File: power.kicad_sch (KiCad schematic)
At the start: 30 parts, among them J7 Conn_01x02, Q1 CSD17311Q5, Q2 CSD17311Q5, Q4 2N7002K, U10 DS4432U+, U8 INA260, U9 TPS40305

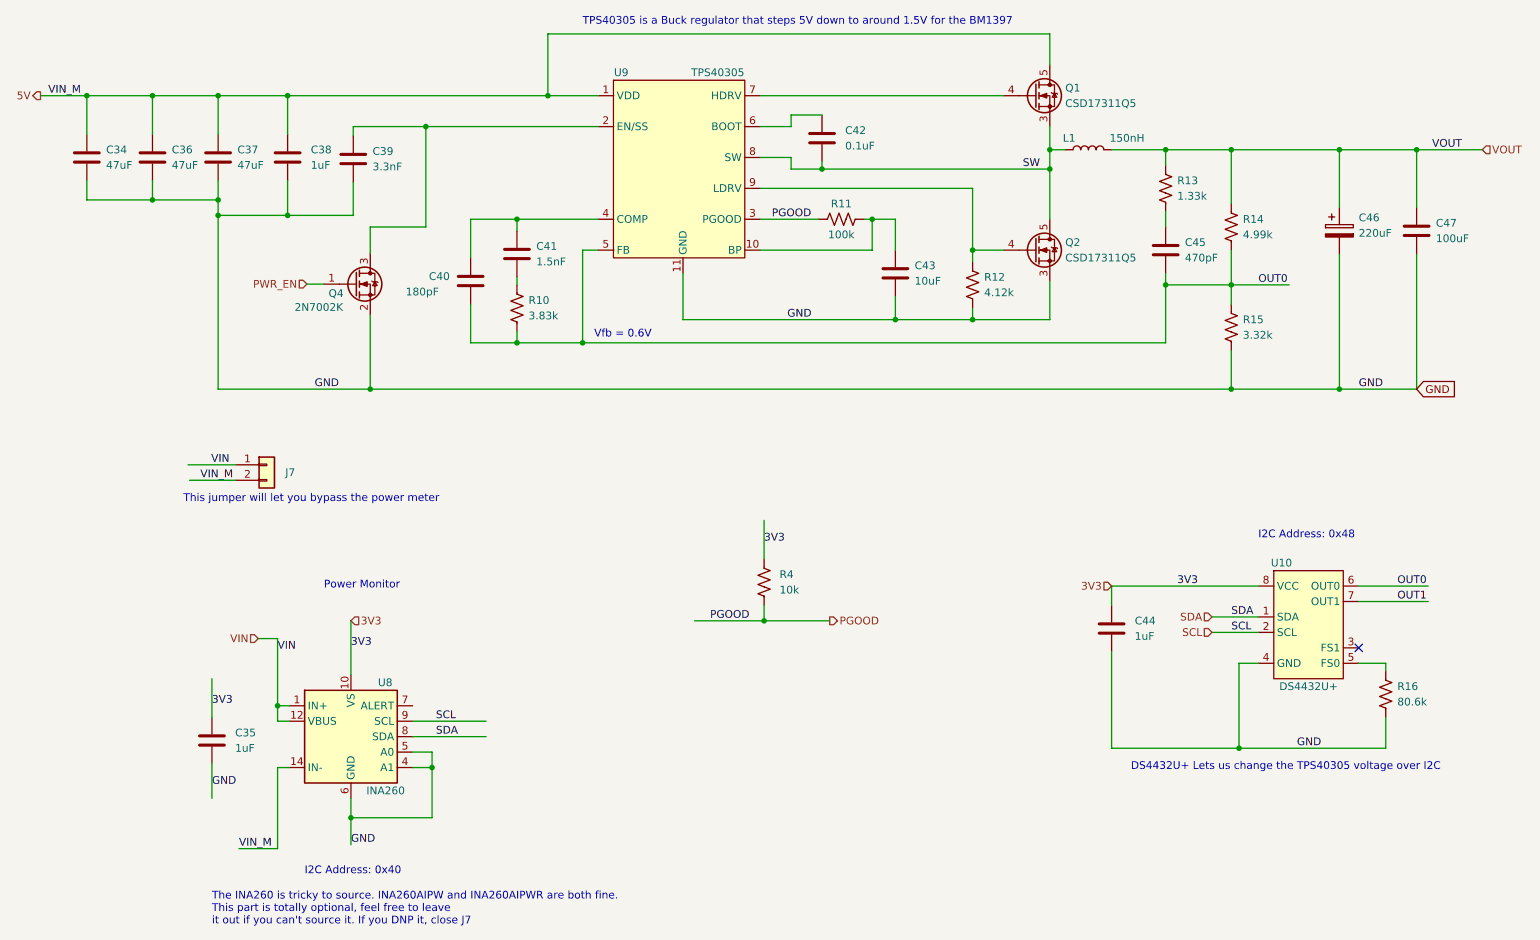
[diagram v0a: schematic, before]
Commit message: added bitaxe variant for rasperry pi
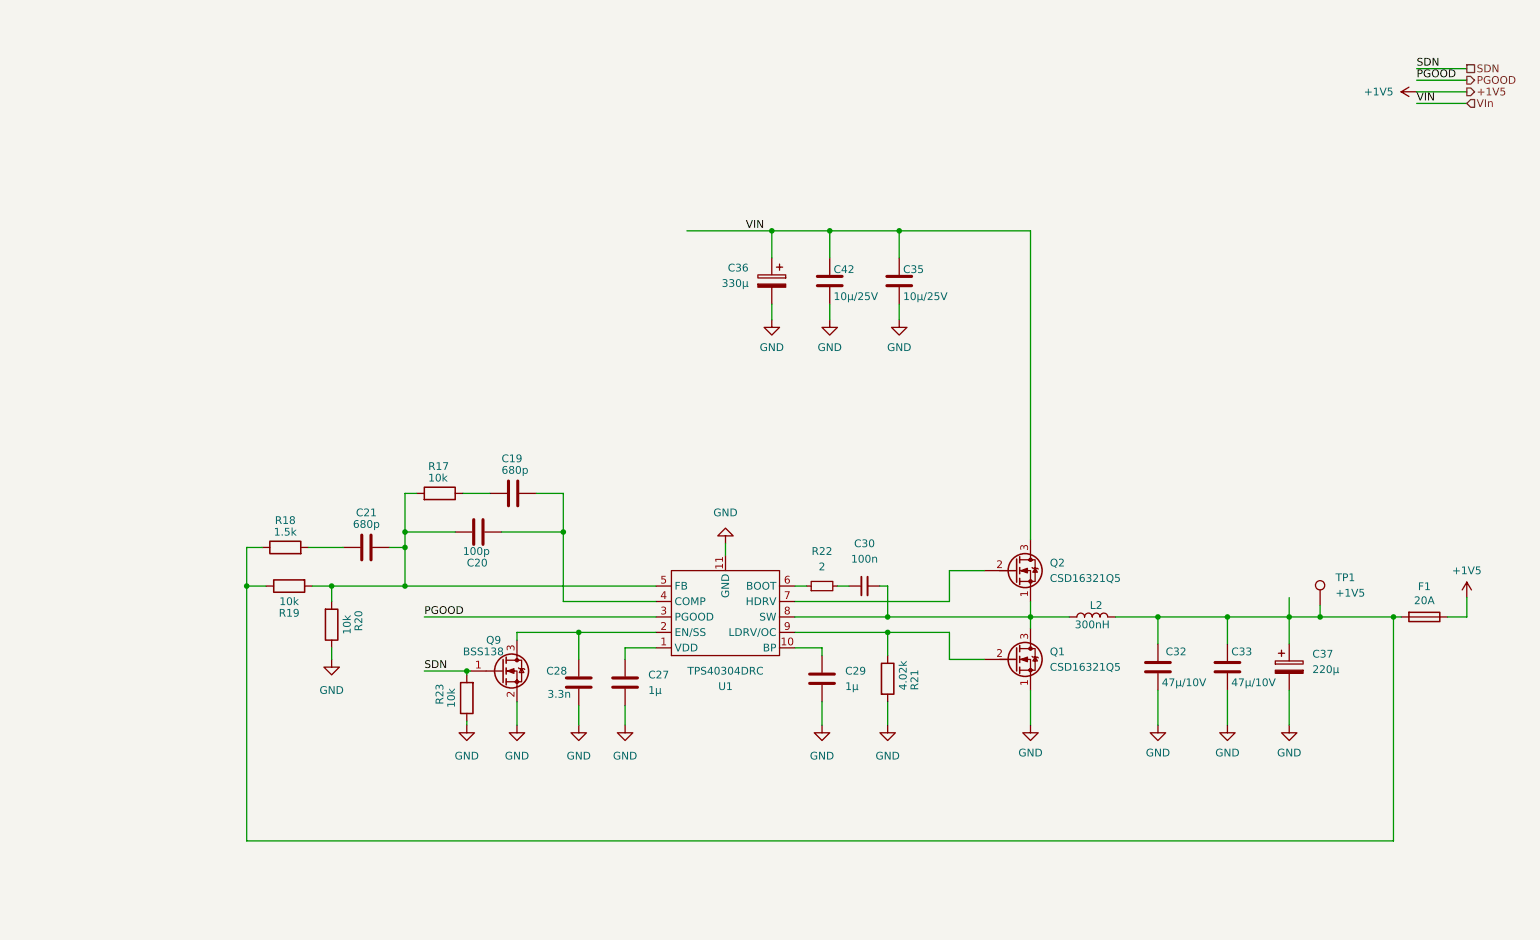
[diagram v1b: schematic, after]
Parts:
- removed C34, C36, C37: 47uF, Capacitor_SMD:C_1210_3225Metric, symbol Device:C
- removed C38: 1uF, Capacitor_SMD:C_0805_2012Metric, symbol Device:C
- removed C39: 3.3nF, Capacitor_SMD:C_0402_1005Metric, symbol Device:C
- removed C40: 180pF, Capacitor_SMD:C_0805_2012Metric, symbol Device:C
- removed C41: 1.5nF, Capacitor_SMD:C_0805_2012Metric, symbol Device:C
- removed C43: 10uF, Capacitor_SMD:C_0805_2012Metric, symbol Device:C
- removed C44: 1uF, Capacitor_SMD:C_0402_1005Metric, symbol Device:C
- removed C45: 470pF, Capacitor_SMD:C_0805_2012Metric, symbol Device:C
- removed C46: 220uF, bitaxe:CAP_2R5TPE220MAFB, symbol Device:C_Polarized
- removed C47: 100uF, Capacitor_SMD:C_1206_3216Metric, symbol Device:C
- removed J7: Conn_01x02, Connector_PinHeader_2.54mm:PinHeader_1x02_P2.54mm_Vertical, symbol Connector_Generic:Conn_01x02
- removed L1: 150nH, bitaxe:FP1005R1-R15-R, symbol Device:L
- removed Q1, Q2: CSD17311Q5, bitaxe:CSD17311Q5, symbol bitaxe:Q_NMOS_CSD17311Q5_1
- removed Q4: 2N7002K, Package_TO_SOT_SMD:SOT-323_SC-70, symbol Transistor_FET:2N7002K
- removed R10: 3.83k, Resistor_SMD:R_0402_1005Metric, symbol Device:R_US
- removed R11: 100k, Resistor_SMD:R_0402_1005Metric, symbol Device:R_US
- removed R12: 4.12k, Resistor_SMD:R_0402_1005Metric, symbol Device:R_US
- removed R13: 1.33k, Resistor_SMD:R_0402_1005Metric, symbol Device:R_US
- removed R14: 4.99k, Resistor_SMD:R_0402_1005Metric, symbol Device:R_US
- removed R15: 3.32k, Resistor_SMD:R_0402_1005Metric, symbol Device:R_US
- removed R16: 80.6k, Resistor_SMD:R_0402_1005Metric, symbol Device:R_US
- removed R4: 10k, Resistor_SMD:R_0402_1005Metric, symbol Device:R_US
- removed U10: DS4432U+, Package_SO:TSSOP-8_3x3mm_P0.65mm, symbol bitaxe:DS4432U+
- removed U8: INA260, Package_SO:TSSOP-16_4.4x5mm_P0.65mm, symbol Sensor:INA260
- removed U9: TPS40305, bitaxe:TPS40305, symbol bitaxe:TPS40305
- added C19, C21: 680p, Capacitor_SMD:C_0805_2012Metric, symbol Device:C
- added C20: 100p, Capacitor_SMD:C_0805_2012Metric, symbol Device:C
- added C27, C29: 1µ, Capacitor_SMD:C_0805_2012Metric, symbol Device:C
- added C28: 3.3n, Capacitor_SMD:C_0805_2012Metric, symbol Device:C
- added C30: 100n, Capacitor_SMD:C_0805_2012Metric, symbol Device:C_Small
- added C32, C33: 47µ/10V, Capacitor_SMD:C_1206_3216Metric, symbol Device:C
- added C36: 330µ, Capacitor_SMD:CP_Elec_8x10, symbol Device:C_Polarized
- added C37: 220µ, Capacitor_SMD:CP_Elec_5x5.8, symbol Device:C_Polarized
- added F1: 20A, myfootprints:fuseholder_littlefuse_blok, symbol Device:Fuse
- added L2: 300nH, Inductor_SMD:L_Bourns_SRP7028A_7.3x6.6mm, symbol Device:L
- added Q1, Q2: CSD16321Q5, Package_SON:VSONP-8-1EP_5x6_P1.27mm, symbol Device:Q_NMOS_SGD
- added Q9: BSS138, Package_TO_SOT_SMD:SOT-23, symbol Transistor_FET:BSS138
- added R17, R19, R20, R23: 10k, Resistor_SMD:R_0805_2012Metric, symbol Device:R
- added R18: 1.5k, Resistor_SMD:R_0805_2012Metric, symbol Device:R
- added R21: 4.02k, Resistor_SMD:R_0805_2012Metric, symbol Device:R
- added R22: 2, Resistor_SMD:R_1206_3216Metric, symbol Device:R_Small
- added TP1: +1V5, TestPoint:TestPoint_Pad_D2.0mm, symbol Connector:TestPoint
- added U1: TPS40304DRC, Package_SON:VSON-10-1EP_3x3mm_P0.5mm_EP1.65x2.4mm_ThermalVias, symbol mylib7:TPS40304
- C35: value 1uF -> 10µ/25V; footprint Capacitor_SMD:C_0402_1005Metric -> Capacitor_SMD:C_1206_3216Metric; DK 587-5514-1-ND -> (none); PARTNO EMK105BJ105MV-F -> (none)
- C42: value 0.1uF -> 10µ/25V; footprint Capacitor_SMD:C_0402_1005Metric -> Capacitor_SMD:C_1206_3216Metric; DK 1292-1639-1-ND -> (none); PARTNO 0402X104K100CT -> (none)
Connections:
- net 3V3 is gone; now on net VIn: C35.1
- net SW is gone; now on net GND: C42.2
- net GND: now also C27.2, C28.2, C29.2, C32.2, C33.2, C36.2, C37.2, Q1.1 (S), Q9.2 (S), R20.1, R21.2, R23.1, U1.11 (GND)
- net PGOOD: now also U1.3 (PGOOD)
- net VIn: now reaches C42.1
- net VIn: now also C36.1, Q2.3 (D)
- new net: C32.1, C33.1, C37.1, F1.2, L2.2, R18.1, R19.1, TP1.1
- new net: C19.1, C20.1, U1.4 (COMP)
- new net: C19.2, R17.1
- new net: C21.1, R18.2
- new net: C29.1, U1.10 (BP)
- new net: C20.2, C21.2, R17.2, R19.2, R20.2, U1.5 (FB)
- new net: C27.1, U1.1 (VDD)
- new net: R22.1, U1.6 (BOOT)
- new net: C30.1, R22.2
- new net: C28.1, Q9.3 (D), U1.2 (EN/SS)
- new net: Q2.2 (G), U1.7 (HDRV)
- new net: C30.2, L2.1, Q1.3 (D), Q2.1 (S), U1.8 (SW)
- new net: Q1.2 (G), R21.1, U1.9 (LDRV/OC)
- new net +1V5: F1.1
- new net SDN: Q9.1 (G), R23.2
- no-connect marks 1 -> 0
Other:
- note removed: "DS4432U+ Lets us change the TPS40305 voltage over I2C"
- note removed: "I2C Address: 0x40"
- note removed: "I2C Address: 0x48"
- note removed: "Power Monitor"
- note removed: "TPS40305 is a Buck regulator that steps 5V down to around 1.5V for the BM1397"
- note removed: "The INA260 is tricky to source. INA260AIPW and INA260AIPWR are both fine. This part is totally optional, feel free to leave it out if you can't source it. If you DNP it, close J7"
- note removed: "This jumper will let you bypass the power meter"
- note removed: "Vfb = 0.6V"
